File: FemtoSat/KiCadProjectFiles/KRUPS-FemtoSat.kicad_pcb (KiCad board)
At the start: 4 copper layers, 29.2 x 71.9 mm, 54 parts, among them J1 B2P-VH-FB-B, J2 B2PS-VH, J3 USB_C_Receptacle_USB2.0_16P, J4 Conn_02x02, Q1 IRF7410, SW1 Enclosure Detector, U1 BME280, U2 ESP32-S3-WROOM-1-N16R8, U3 TSR_2-2450, U4 TPS61023, U5 E22-900M33S, U6 TPS2117, U8 BNO086, U9 AZ1117-3.3

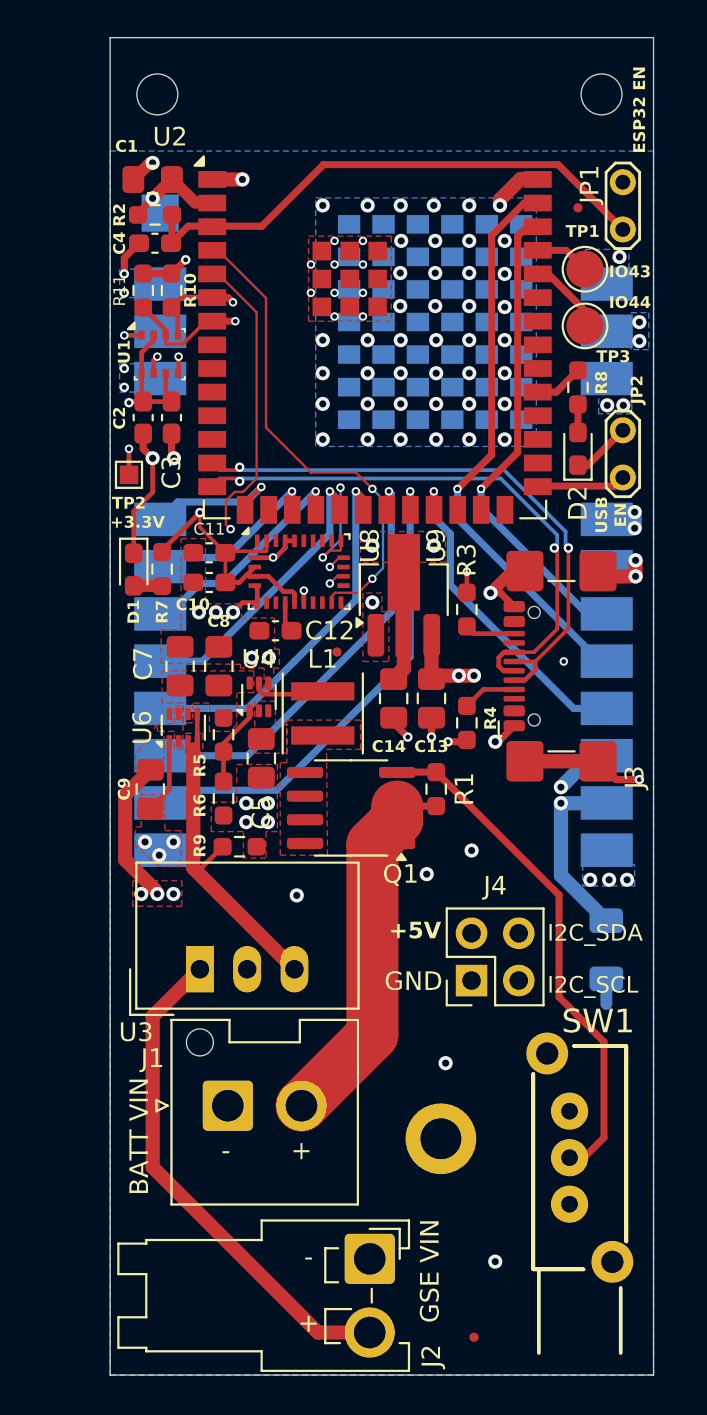
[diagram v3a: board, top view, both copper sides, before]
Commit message: Changed to Raspi Pico, 1W radio
- Swapped the ESP32 S3 WROOM to a Raspberry Pi Pico 2 W on both the FemtoSat and RocketStation
- Swapped to 1W LoRa module in place of the 2W EBYTE one
- bunch of layout, documentation, miscellaneous changes
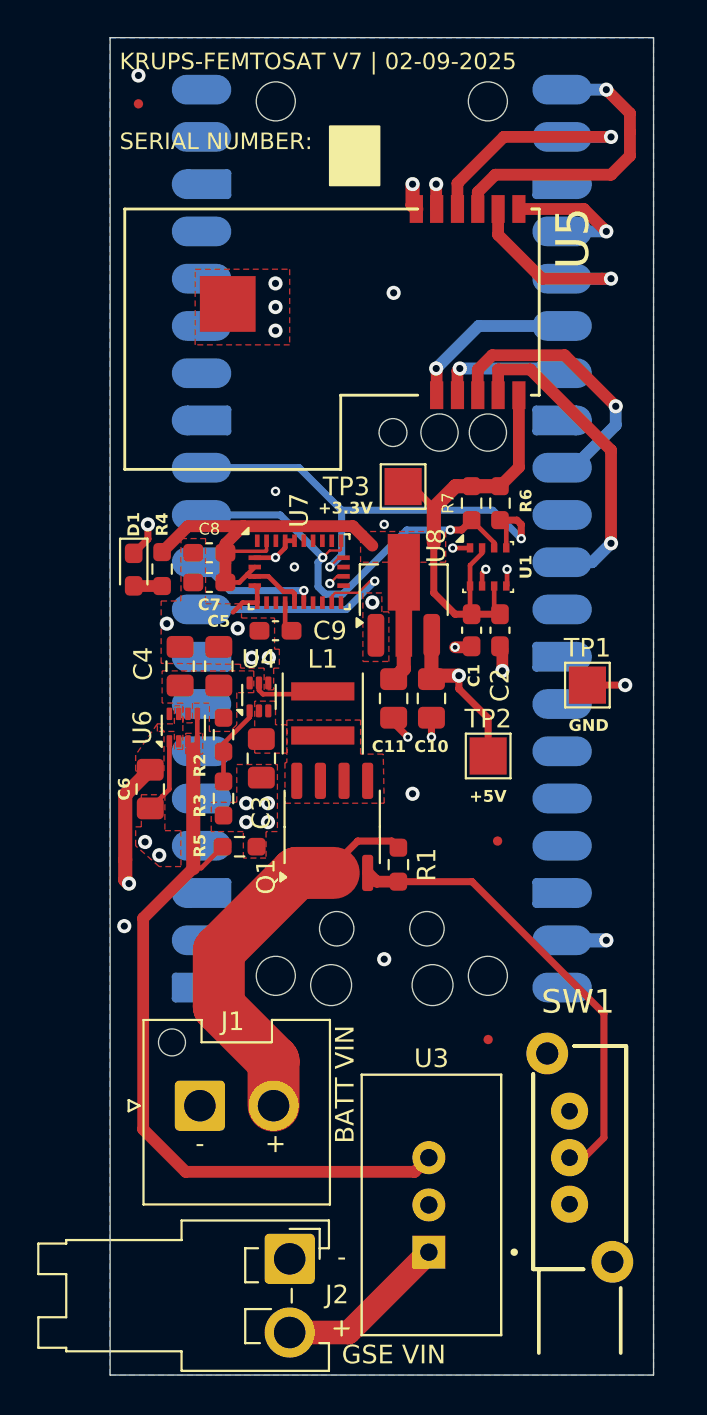
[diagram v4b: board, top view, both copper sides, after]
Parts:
- removed the C1 at (91.2, 29.7)
- removed the C4 at (91.3, 33.1)
- removed the C6 at (115.6, 71.1)
- removed D2: LED, Diode_SMD:D_0603_1608Metric_Pad1.05x0.95mm_HandSolder
- removed H1, H2: MountingHole, MountingHole:MountingHole_2.2mm_M2
- removed H3: MountingHole, MountingHole:MountingHole_2.2mm_M2_DIN965_Pad
- removed J3: USB_C_Receptacle_USB2.0_16P, Connector_USB:USB_C_Receptacle_GCT_USB4110
- removed J4: Conn_02x02, Connector_PinHeader_2.54mm:PinHeader_2x02_P2.54mm_Vertical
- removed JP1, JP2: Jumper_2_Small_Open, TestPoint:TestPoint_2Pads_Pitch2.54mm_Drill0.8mm
- removed the R2 at (91.3, 31.6)
- removed the R3 at (108.1, 52.8)
- removed the R4 at (108.1, 58.9)
- removed R8: 68, Resistor_SMD:R_0603_1608Metric_Pad0.98x0.95mm_HandSolder
- removed the TP3 at (114.4, 37.6)
- removed TP4: TestPoint, TestPoint:TestPoint_Pad_2.0x2.0mm
- added TP2: +5V, TestPoint:TestPoint_Pad_2.0x2.0mm, F.Cu at (109.2, 60.7)
- TP1: value TestPoint -> GND; footprint TestPoint:TestPoint_Pad_D2.0mm -> TestPoint:TestPoint_Pad_2.0x2.0mm
- TP3: renamed from TP2; footprint TestPoint:TestPoint_Pad_1.0x1.0mm -> TestPoint:TestPoint_Pad_2.0x2.0mm
- U2: value ESP32-S3-WROOM-1-N16R8 -> Pico_2_W; footprint RF_Module:ESP32-S3-WROOM-2 -> KRUPS-FemtoSat:RaspberryPi_Pico2_W_SMD; moved to B.Cu
- U3: footprint Converter_DCDC:Converter_DCDC_TRACO_TSR-1_THT -> KRUPS-FemtoSat:CONV_TSR_2-2450
- U5: value E22-900M33S -> LR62XE; footprint KRUPS-FemtoSat:E22-XXXM33S -> KRUPS-FemtoSat:LR62XE; moved to F.Cu
- moved FID2 24.3 mm to (90.4, 25.7)
- moved TP1 22.4 mm to (114.6, 56.9)
- moved C1 21.0 mm to (108.3, 53.9)
- moved C2 21.0 mm to (109.9, 53.9)
- moved R6 21.0 mm to (109.9, 47.1)
- moved R7 21.0 mm to (108.3, 47.1)
- moved U1 21.0 mm to (109.2, 50.5)
- moved U3 17.8 mm to (106.2, 84.8), turned to 90 degrees
- moved FID1 16.0 mm to (109.2, 75.9)
- moved TP3 14.7 mm to (104.6, 46.2)
- moved U2 14.0 mm to (103.5, 49.0)
- moved FID3 13.3 mm to (109.7, 65.3)
- moved U5 12.3 mm to (112.0, 41.3)
- moved R1 4.54 mm to (104.4, 66.5), turned to -90 degrees
- moved J2 4.30 mm to (98.6, 87.7)
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- renumbered C2 to C1, C13 to C10, C14 to C11, C3 to C2, C5 to C3, C7 to C4, C8 to C5, C9 to C6, C10 to C7, C11 to C8, C12 to C9, R5 to R2, R6 to R3, R7 to R4, R9 to R5, R10 to R6, R11 to R7, U8 to U7, U9 to U8
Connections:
- TP1 pad 1: /IO43 -> GND
- U2 pad 1: GND -> unconnected-(U2-GPIO0-Pad1)
- U2 pad 10: unconnected-(U2-IO17-Pad10) -> /~{BNO086_RESET}
- U2 pad 11: unconnected-(U2-IO18-Pad11) -> /I2C_SDA
- U2 pad 12: unconnected-(U2-IO8-Pad12) -> /I2C_SCL
- U2 pad 13: /USB_D- -> GND
- U2 pad 14: /USB_D+ -> unconnected-(U2-GPIO10-Pad14)
- U2 pad 15: /SPI_NSS -> unconnected-(U2-GPIO11-Pad15)
- U2 pad 17: /SPI_CLK -> unconnected-(U2-GPIO13-Pad17)
- U2 pad 18: /SPI_MOSI -> GND
- U2 pad 19: /SPI_MISO -> unconnected-(U2-GPIO14-Pad19)
- U2 pad 2: +3V3 -> unconnected-(U2-GPIO1-Pad2)
- U2 pad 20: /~{LORA_RESET} -> unconnected-(U2-GPIO15-Pad20)
- U2 pad 21: /LORA_BUSY -> /SPI_MISO
- U2 pad 22: /LORA_DIO1 -> /SPI_NSS
- U2 pad 23: /LORA_DIO2 -> GND
- U2 pad 24: unconnected-(U2-IO47-Pad24) -> /SPI_CLK
- U2 pad 25: unconnected-(U2-IO48-Pad25) -> /SPI_MOSI
- U2 pad 26: unconnected-(U2-IO45-Pad26) -> /LORA_ANTSW
- U2 pad 27: /USB_EN -> /~{LORA_RESET}
- U2 pad 28: unconnected-(U2-NC-Pad28) -> GND
- U2 pad 29: unconnected-(U2-NC-Pad29) -> /LORA_BUSY
- U2 pad 3: /ESP32_EN -> GND
- U2 pad 31: /GPIO_LED -> /LORA_DIO1
- U2 pad 33: unconnected-(U2-MTDO/IO40-Pad33) -> GND
- U2 pad 36: /IO44 -> unconnected-(U2-3V3-Pad36)
- U2 pad 37: /IO43 -> unconnected-(U2-3V3_EN-Pad37)
- U2 pad 38: /LORA_RXEN -> GND
- U2 pad 39: /LORA_TXEN -> +5V
- U2 pad 4: /BNO086_HINTN -> unconnected-(U2-GPIO2-Pad4)
- U2 pad 40: GND -> unconnected-(U2-VBUS-Pad40)
- U2 pad 5: /~{BNO086_RESET} -> unconnected-(U2-GPIO3-Pad5)
- U2 pad 6: /I2C_SCL -> unconnected-(U2-GPIO4-Pad6)
- U2 pad 7: /I2C_SDA -> unconnected-(U2-GPIO5-Pad7)
- U2 pad 8: unconnected-(U2-IO15-Pad8) -> GND
- U2 pad 9: unconnected-(U2-IO16-Pad9) -> /BNO086_HINTN
- U5 pad 1: GND -> /LORA_ANTSW
- U5 pad 10: +5V -> GND
- U5 pad 11: GND -> +5V
- U5 pad 2: GND -> /~{LORA_RESET}
- U5 pad 3: GND -> /LORA_BUSY
- U5 pad 4: GND -> /LORA_DIO1
- U5 pad 5: GND -> +3V3
- U5 pad 6: /LORA_RXEN -> /SPI_CLK
- U5 pad 7: /LORA_TXEN -> /SPI_MOSI
- U5 pad 8: /LORA_DIO2 -> /SPI_MISO
- U5 pad 9: +5V -> /SPI_NSS
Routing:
- net GND: track 62.4 -> 22.9 mm, vias 103 -> 34
- net /I2C_SCL: track 62.9 -> 26.6 mm
- net +5V: track 67.8 -> 102.3 mm, vias 7 -> 4
- net /USB_D-: track 31.4 -> 0.00 mm, vias 2 -> 0
- net /I2C_SDA: track 53.7 -> 22.8 mm, vias 3 -> 2
- net /USB_D+: track 30.5 -> 0.00 mm, vias 2 -> 0
- net /LORA_TXEN: track 30.4 -> 0.00 mm, vias 1 -> 0
- net /ESP32_EN: track 29.3 -> 0.00 mm
- net /LORA_RXEN: track 25.8 -> 0.00 mm, vias 1 -> 0
- net /5V_GSE: track 17.6 -> 41.7 mm
- net +3V3: track 71.5 -> 52.2 mm, vias 7 -> 0
- net /GSE_VIN: track 27.0 -> 9.27 mm
- net /LORA_DIO2: track 17.5 -> 0.00 mm, vias 1 -> 0
- net /~{BNO086_RESET}: track 21.6 -> 6.78 mm, vias 2 -> 1
- net /BNO086_HINTN: track 26.3 -> 12.9 mm, vias 2 -> 1
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- removed copper zone on In1.Cu, net +5V
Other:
- board text added: "KRUPS-FEMTOSAT V7 | 02-09-2025 SERIAL NUMBER:"
- board text removed: "ESP32 EN"
- board text removed: "I2C_SCL"
- board text removed: "I2C_SDA"
- board text removed: "IO43"
- board text removed: "IO44"
- board text removed: "KRUPS-FEMTOSAT V6 | 12-28-2024 SERIAL NUMBER:"
- board text removed: "PCB Antenna"
- board text removed: "USB EN"
